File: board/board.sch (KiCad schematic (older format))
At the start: 16 parts, among them J1 MOTION DETECTOR, J2 EXT BUTTON, U3 ATTINY85-20PU

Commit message: Revision
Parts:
- R1: value 22.6K -> 22.1K
- R4, R8: footprint (none) -> Resistors_SMD:R_0805_HandSoldering
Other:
- moved on the sheet: J1, R7
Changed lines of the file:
@@
 Adafruit FeatherWing\n
 $Comp
-L VCC #PWR14
+L VCC #PWR01
 U 1 1 56D753B8
 P 9700 750
-F 0 "#PWR14" H 9700 600 50  0001 C CNN
+F 0 "#PWR01" H 9700 600 50  0001 C CNN
 F 1 "VCC" H 9700 900 50  0000 C CNN
 F 2 "" H 9700 750 50  0000 C CNN
@@
 	1    10250 1650
 	1    0    0    1
-$EndComp
-$Comp
-L GND #PWR15
-U 1 1 56D75A03
-P 9700 2500
-F 0 "#PWR15" H 9700 2250 50  0001 C CNN
-F 1 "GND" H 9700 2350 50  0000 C CNN
-F 2 "" H 9700 2500 50  0000 C CNN
-F 3 "" H 9700 2500 50  0000 C CNN
-	1    9700 2500
-	1    0    0    -1
 $EndComp
 Text Label 10050 900  2    60   ~ 0
@@
 VUSB
 NoConn ~ 10050 2400
-$Comp
-L GND #PWR11
-U 1 1 59796D2F
-P 8150 3800
-F 0 "#PWR11" H 8150 3550 50  0001 C CNN
-F 1 "GND" H 8150 3650 50  0000 C CNN
-F 2 "" H 8150 3800 50  0001 C CNN
-F 3 "" H 8150 3800 50  0001 C CNN
-	1    8150 3800
-	1    0    0    -1
-$EndComp
 Text Label 8800 3200 0    60   ~ 0
 VBAT
@@
 L CONN_01X03 J1
 U 1 1 59797A62
-P 7650 750
-F 0 "J1" H 7650 950 50  0000 C CNN
-F 1 "MOTION DETECTOR" V 7750 750 50  0000 C CNN
-F 2 "Pin_Headers:Pin_Header_Angled_1x03_Pitch2.54mm" H 7650 750 50  0001 C CNN
-F 3 "" H 7650 750 50  0001 C CNN
-	1    7650 750
+P 7600 850
+F 0 "J1" H 7600 1050 50  0000 C CNN
+F 1 "MOTION DETECTOR" V 7700 850 50  0000 C CNN
+F 2 "Pin_Headers:Pin_Header_Angled_1x03_Pitch2.54mm" H 7600 850 50  0001 C CNN
+F 3 "" H 7600 850 50  0001 C CNN
+	1    7600 850
 	0    -1   -1   0
 $EndComp
@@
 P 6250 1400
 F 0 "R1" V 6150 1400 50  0000 C CNN
-F 1 "22.6K" V 6250 1400 39  0000 C CNN
+F 1 "22.1K" V 6250 1400 39  0000 C CNN
 F 2 "Resistors_SMD:R_0805_HandSoldering" V 6180 1400 50  0001 C CNN
 F 3 "" H 6250 1400 50  0001 C CNN
@@
 Connection ~ 6250 1600
 $Comp
-L GND #PWR6
+L GND #PWR02
 U 1 1 597CE63C
 P 6250 2000
-F 0 "#PWR6" H 6250 1750 50  0001 C CNN
+F 0 "#PWR02" H 6250 1750 50  0001 C CNN
 F 1 "GND" H 6250 1850 50  0000 C CNN
 F 2 "" H 6250 2000 50  0001 C CNN
@@
 $EndComp
 $Comp
-L VCC #PWR5
+L VCC #PWR03
 U 1 1 597CEF49
 P 6250 1250
-F 0 "#PWR5" H 6250 1100 50  0001 C CNN
+F 0 "#PWR03" H 6250 1100 50  0001 C CNN
 F 1 "VCC" H 6250 1400 50  0000 C CNN
 F 2 "" H 6250 1250 50  0001 C CNN
@@
 A0
 $Comp
-L GND #PWR7
+L GND #PWR04
 U 1 1 597D0A0F
 P 6650 2000
-F 0 "#PWR7" H 6650 1750 50  0001 C CNN
+F 0 "#PWR04" H 6650 1750 50  0001 C CNN
 F 1 "GND" H 6650 1850 50  0000 C CNN
 F 2 "" H 6650 2000 50  0001 C CNN
@@
 Connection ~ 6650 1600
 $Comp
-L GND #PWR12
+L GND #PWR05
 U 1 1 597D0EF3
 P 8250 2450
-F 0 "#PWR12" H 8250 2200 50  0001 C CNN
+F 0 "#PWR05" H 8250 2200 50  0001 C CNN
 F 1 "GND" H 8250 2300 50  0000 C CNN
 F 2 "" H 8250 2450 50  0001 C CNN
@@
 $EndComp
 $Comp
-L GND #PWR4
+L GND #PWR06
 U 1 1 597D2087
 P 5800 2000
-F 0 "#PWR4" H 5800 1750 50  0001 C CNN
+F 0 "#PWR06" H 5800 1750 50  0001 C CNN
 F 1 "GND" H 5800 1850 50  0000 C CNN
 F 2 "" H 5800 2000 50  0001 C CNN
@@
 $EndComp
 $Comp
-L GND #PWR9
-U 1 1 597D1088
-P 7100 3650
-F 0 "#PWR9" H 7100 3400 50  0001 C CNN
-F 1 "GND" H 7100 3500 50  0000 C CNN
-F 2 "" H 7100 3650 50  0001 C CNN
-F 3 "" H 7100 3650 50  0001 C CNN
-	1    7100 3650
-	1    0    0    -1
-$EndComp
-$Comp
 L AVR-ISP-6 ISP1
 U 1 1 597D1114
@@
 	4300 4050 4300 3350
 Wire Wire Line
-	3400 3350 4400 3350
-$Comp
-L GND #PWR3
+	3850 3350 4400 3350
+$Comp
+L GND #PWR07
 U 1 1 597D12FA
 P 5200 4150
-F 0 "#PWR3" H 5200 3900 50  0001 C CNN
+F 0 "#PWR07" H 5200 3900 50  0001 C CNN
 F 1 "GND" H 5200 4000 50  0000 C CNN
 F 2 "" H 5200 4150 50  0001 C CNN
@@
 	5200 4150 4850 4150
 Wire Wire Line
-	4850 3950 5450 3950
-Wire Wire Line
 	4400 3250 4200 3250
 Wire Wire Line
@@
 	4200 3950 4600 3950
 Wire Wire Line
-	4000 3150 4000 4400
-Wire Wire Line
-	3400 3150 4400 3150
-Wire Wire Line
-	4850 4050 5300 4050
-Wire Wire Line
-	5300 4050 5300 4400
-Wire Wire Line
-	5300 4400 4000 4400
+	3850 3150 4400 3150
+Wire Wire Line
+	4850 4050 5450 4050
 Wire Wire Line
 	4400 3550 3400 3550
@@
 Text Label 2800 3450 0    60   ~ 0
 ~RESET
-Text Label 7550 2000 1    60   ~ 0
+Text Label 7500 2100 1    60   ~ 0
 MOTION_GND
 Wire Wire Line
-	7550 2000 7550 950
-Wire Wire Line
-	7650 2000 7650 950
-Wire Wire Line
-	7750 1050 7750 950
-Text Label 7650 2000 1    60   ~ 0
+	7500 2100 7500 1050
+Wire Wire Line
+	7600 2100 7600 1050
+Wire Wire Line
+	7700 1150 7700 1050
+Text Label 7600 2100 1    60   ~ 0
 MOTION_VCC
-Text Label 7750 2000 1    60   ~ 0
+Text Label 7700 2100 1    60   ~ 0
 MOTION_SIG
 Text Label 8100 2450 1    60   ~ 0
@@
 	8100 2450 8100 1850
 $Comp
-L VCC #PWR10
+L VCC #PWR08
 U 1 1 597D3E37
 P 8100 1850
-F 0 "#PWR10" H 8100 1700 50  0001 C CNN
+F 0 "#PWR08" H 8100 1700 50  0001 C CNN
 F 1 "VCC" H 8100 2000 50  0000 C CNN
 F 2 "" H 8100 1850 50  0001 C CNN
@@
 Text Label 3400 3550 0    60   ~ 0
 MOTION_SIG
-Text Label 5450 3950 2    60   ~ 0
-VCC
 $Comp
 L R R5
@@
 L R R7
 U 1 1 5982A87C
-P 7750 1200
-F 0 "R7" V 7830 1200 50  0000 C CNN
-F 1 "1K" V 7750 1200 50  0000 C CNN
-F 2 "Resistors_SMD:R_0805_HandSoldering" V 7680 1200 50  0001 C CNN
-F 3 "" H 7750 1200 50  0001 C CNN
-	1    7750 1200
-	1    0    0    -1
-$EndComp
-Wire Wire Line
-	7750 2000 7750 1350
-$Comp
-L GND #PWR13
+P 7700 1300
+F 0 "R7" V 7780 1300 50  0000 C CNN
+F 1 "1K" V 7700 1300 50  0000 C CNN
+F 2 "Resistors_SMD:R_0805_HandSoldering" V 7630 1300 50  0001 C CNN
+F 3 "" H 7700 1300 50  0001 C CNN
+	1    7700 1300
+	1    0    0    -1
+$EndComp
+Wire Wire Line
+	7700 2100 7700 1450
+$Comp
+L GND #PWR09
 U 1 1 5986A206
 P 9250 3800
-F 0 "#PWR13" H 9250 3550 50  0001 C CNN
+F 0 "#PWR09" H 9250 3550 50  0001 C CNN
 F 1 "GND" H 9250 3650 50  0000 C CNN
 F 2 "" H 9250 3800 50  0001 C CNN
@@
 	1    0    0    -1
 $EndComp
-$Comp
-L VCC #PWR8
-U 1 1 5987EE9E
-P 7100 3150
-F 0 "#PWR8" H 7100 3000 50  0001 C CNN
-F 1 "VCC" H 7100 3300 50  0000 C CNN
-F 2 "" H 7100 3150 50  0001 C CNN
-F 3 "" H 7100 3150 50  0001 C CNN
-	1    7100 3150
-	1    0    0    -1
-$EndComp
 Wire Wire Line
 	6250 1600 6650 1600
-Connection ~ 4000 3150
 Connection ~ 4300 3350
-Text Label 3400 3350 0    60   ~ 0
+Text Label 3850 3350 0    60   ~ 0
 SCL
-Text Label 3400 3150 0    60   ~ 0
+Text Label 3850 3150 0    60   ~ 0
 SDA
 $Comp
-L VCC #PWR2
+L VCC #PWR010
 U 1 1 598F5087
 P 3250 3800
-F 0 "#PWR2" H 3250 3650 50  0001 C CNN
+F 0 "#PWR010" H 3250 3650 50  0001 C CNN
 F 1 "VCC" H 3250 3950 50  0000 C CNN
 F 2 "" H 3250 3800 50  0001 C CNN
@@
 SCL
 $Comp
-L VCC #PWR1
+L VCC #PWR011
 U 1 1 598F54B3
 P 3050 3800
-F 0 "#PWR1" H 3050 3650 50  0001 C CNN
+F 0 "#PWR011" H 3050 3650 50  0001 C CNN
 F 1 "VCC" H 3050 3950 50  0000 C CNN
 F 2 "" H 3050 3800 50  0001 C CNN
@@
 F 0 "R4" V 3130 3950 50  0000 C CNN
 F 1 "4.7K" V 3050 3950 50  0000 C CNN
-F 2 "" V 2980 3950 50  0001 C CNN
+F 2 "Resistors_SMD:R_0805_HandSoldering" V 2980 3950 50  0001 C CNN
 F 3 "" H 3050 3950 50  0001 C CNN
 	1    3050 3950
@@
 F 0 "R8" V 3330 3950 50  0000 C CNN
 F 1 "4.7K" V 3250 3950 50  0000 C CNN
-F 2 "" V 3180 3950 50  0001 C CNN
+F 2 "Resistors_SMD:R_0805_HandSoldering" V 3180 3950 50  0001 C CNN
 F 3 "" H 3250 3950 50  0001 C CNN
 	1    3250 3950
 	1    0    0    -1
 $EndComp
+$Comp
+L GND #PWR012
+U 1 1 598F5F5D
+P 8150 3800
+F 0 "#PWR012" H 8150 3550 50  0001 C CNN
+F 1 "GND" H 8150 3650 50  0000 C CNN
+F 2 "" H 8150 3800 50  0001 C CNN
+F 3 "" H 8150 3800 50  0001 C CNN
+	1    8150 3800
+	1    0    0    -1
+$EndComp
+$Comp
+L GND #PWR013
+U 1 1 598F5FE9
+P 7100 3650
+F 0 "#PWR013" H 7100 3400 50  0001 C CNN
+F 1 "GND" H 7100 3500 50  0000 C CNN
+F 2 "" H 7100 3650 50  0001 C CNN
+F 3 "" H 7100 3650 50  0001 C CNN
+	1    7100 3650
+	1    0    0    -1
+$EndComp
+Wire Wire Line
+	4850 3950 5200 3950
+$Comp
+L VCC #PWR014
+U 1 1 598F615B
+P 5200 3950
+F 0 "#PWR014" H 5200 3800 50  0001 C CNN
+F 1 "VCC" H 5200 4100 50  0000 C CNN
+F 2 "" H 5200 3950 50  0001 C CNN
+F 3 "" H 5200 3950 50  0001 C CNN
+	1    5200 3950
+	1    0    0    -1
+$EndComp
+$Comp
+L VCC #PWR015
+U 1 1 598F61A2
+P 7100 3150
+F 0 "#PWR015" H 7100 3000 50  0001 C CNN
+F 1 "VCC" H 7100 3300 50  0000 C CNN
+F 2 "" H 7100 3150 50  0001 C CNN
+F 3 "" H 7100 3150 50  0001 C CNN
+	1    7100 3150
+	1    0    0    -1
+$EndComp
+$Comp
+L GND #PWR016
+U 1 1 598F622C
+P 9700 2500
+F 0 "#PWR016" H 9700 2250 50  0001 C CNN
+F 1 "GND" H 9700 2350 50  0000 C CNN
+F 2 "" H 9700 2500 50  0001 C CNN
+F 3 "" H 9700 2500 50  0001 C CNN
+	1    9700 2500
+	1    0    0    -1
+$EndComp
+Text Label 5450 4050 2    60   ~ 0
+SDA
 $EndSCHEMATC

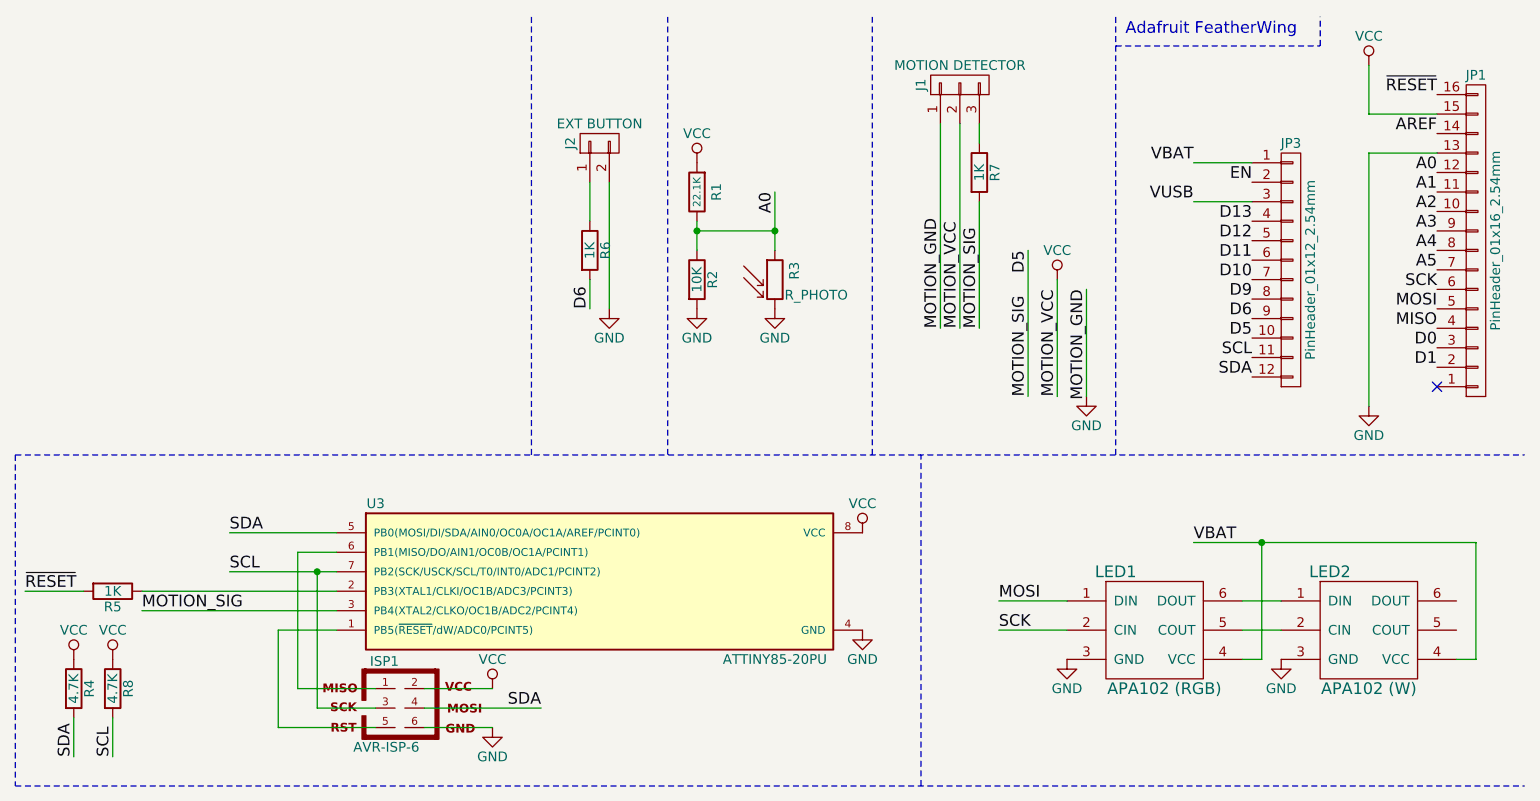
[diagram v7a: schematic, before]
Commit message: Add power button and GPIO16 reset jumper
* Remove redundant resistors
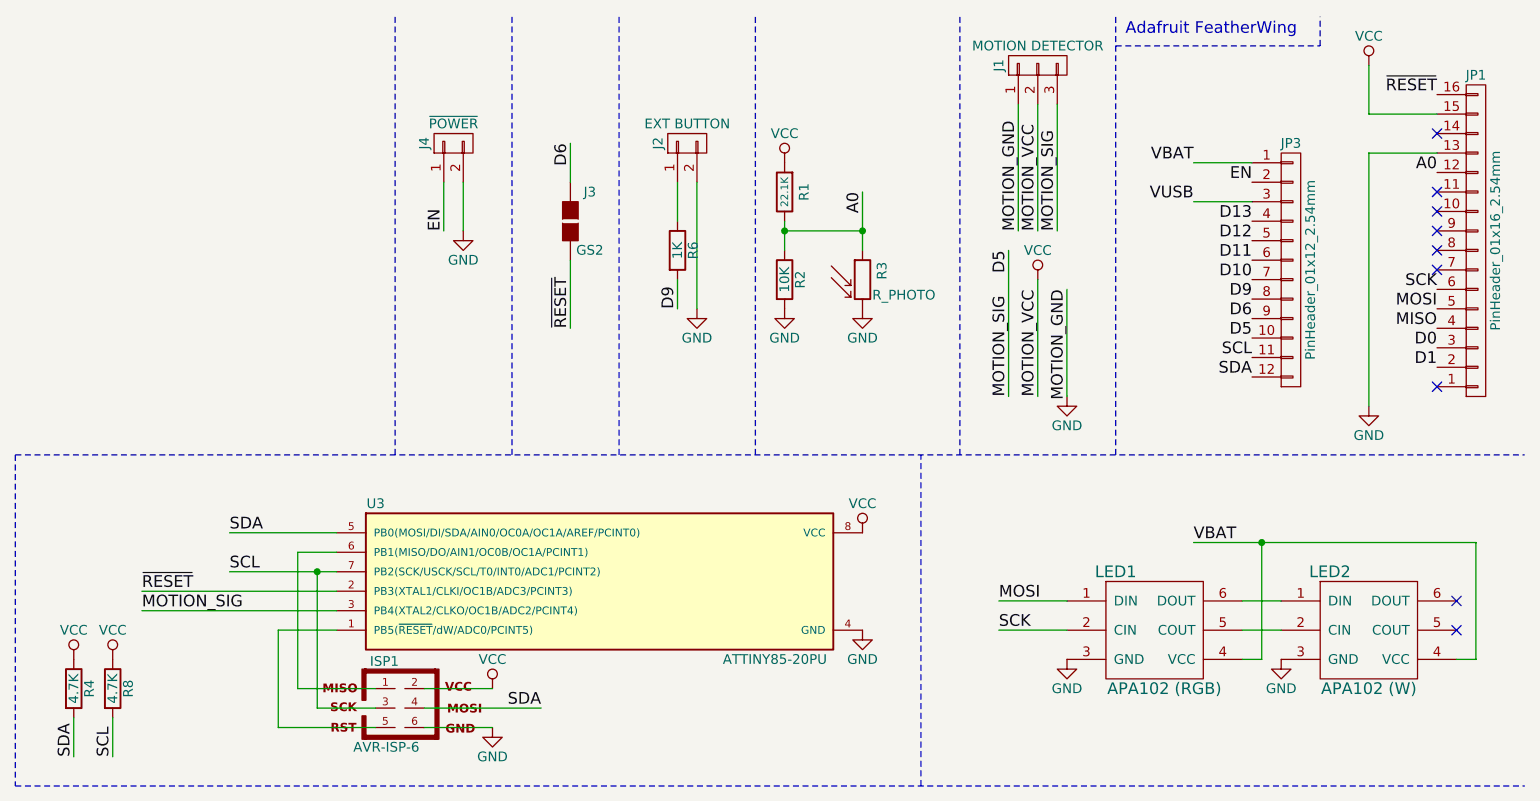
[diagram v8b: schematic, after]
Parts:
- removed R5, R7: 1K, Resistors_SMD:R_0805_HandSoldering, symbol R
- added J3: GS2, Connectors:GS2, symbol GS2
- added J4: ~POWER, Pin_Headers:Pin_Header_Straight_1x02_Pitch2.54mm, symbol CONN_01X02
- R1: MFR (none) -> Stackpole; MPN (none) -> RNCP0805FTD22K1; SPN (none) -> RNCP0805FTD22K1CT-ND; SPR (none) -> Digikey
- R2: MFR (none) -> Stackpole; MPN (none) -> RNCP0805FTD10K0; SPN (none) -> RNCP0805FTD10K0CT-ND; SPR (none) -> Digikey
- R4, R8: MFR (none) -> Stackpole; MPN (none) -> RNCP0805FTD4K75; SPN (none) -> RNCP0805FTD4K75CT-ND; SPR (none) -> Digikey
- R6: MFR (none) -> Stackpole; MPN (none) -> RNCP0805FTD1K00; SPN (none) -> RNCP0805FTD1K00CT-ND; SPR (none) -> Digikey
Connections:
- net D5: now also J1.3 (P3)
- net D6: now also J3.1 (G1); no longer R6.2
- net D9: now also R6.2
- net EN: now also J4.1 (P1)
- net GND: now also J4.2 (P2)
- net ~RESET: now also U3.2 (PB3(XTAL1/CLKI/OC1B/ADC3/PCINT3)), J3.2 (G2)
- net A1: no longer names the net of JP1.11 (P11)
- net A2: no longer names the net of JP1.10 (P10)
- net A3: no longer names the net of JP1.9 (P9)
- net A4: no longer names the net of JP1.8 (P8)
- net A5: no longer names the net of JP1.7 (P7)
- net AREF: no longer names the net of JP1.14 (P14)
- no-connect marks 1 -> 9
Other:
- moved on the sheet: J1, J2, R1, R2, R3, R6
